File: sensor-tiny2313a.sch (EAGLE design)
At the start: 36 parts, among them M1 NRF24L01P-M, M2 DHT22-NP, Q2 IRLML2502, U1 TINY2313-*S*, U2 MCP1640C, X1 I2C, X2 serial

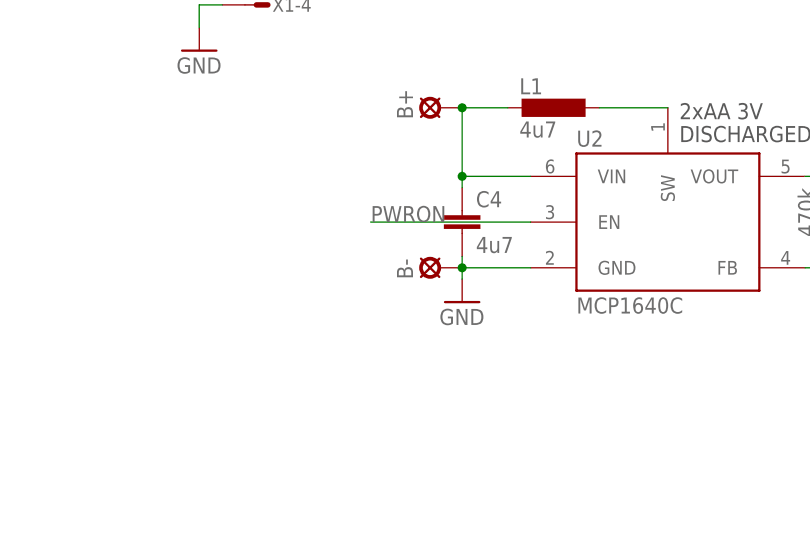
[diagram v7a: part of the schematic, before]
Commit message: pulldown for boostup enable line
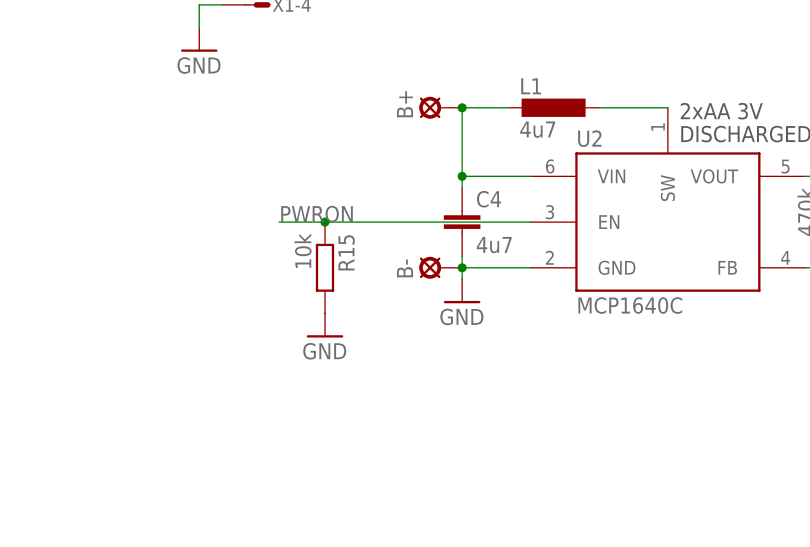
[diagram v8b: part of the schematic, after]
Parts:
- added R15: 10k, rcl:R-EU_R0603
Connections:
- net GND: now also R15.2
- net PWRON: now also R15.1
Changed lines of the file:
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@@
 <part name="U$3" library="creative-commons" deviceset="BY" device="-TPLACE-HS" value="BY-TPLACE-HS"/>
 <part name="U$4" library="creative-commons" deviceset="SA" device="-TPLACE-HALF" value="SA-TPLACE-HALF"/>
+<part name="R15" library="rcl" deviceset="R-EU_" device="R0603" value="10k"/>
+<part name="GND9" library="supply1" deviceset="GND" device=""/>
 </parts>
 <sheets>
@@
 <instance part="U$3" gate="G$1" x="222.25" y="20.32"/>
 <instance part="U$4" gate="G$1" x="227.33" y="20.32"/>
+<instance part="R15" gate="G$1" x="134.62" y="43.18" rot="R270"/>
+<instance part="GND9" gate="1" x="134.62" y="35.56"/>
 </instances>
 <busses>
@@
 <wire x1="120.65" y1="72.39" x2="120.65" y2="69.85" width="0.1524" layer="91"/>
 <pinref part="X1" gate="-4" pin="S"/>
+</segment>
+<segment>
+<pinref part="R15" gate="G$1" pin="2"/>
+<pinref part="GND9" gate="1" pin="GND"/>
 </segment>
 </net>
@@
 <segment>
 <pinref part="U2" gate="G$1" pin="EN"/>
-<wire x1="157.48" y1="48.26" x2="139.7" y2="48.26" width="0.1524" layer="91"/>
-<label x="139.7" y="48.26" size="1.778" layer="95"/>
-</segment>
-<segment>
+<wire x1="157.48" y1="48.26" x2="134.62" y2="48.26" width="0.1524" layer="91"/>
+<label x="129.54" y="48.26" size="1.778" layer="95"/>
+<pinref part="R15" gate="G$1" pin="1"/>
+<wire x1="134.62" y1="48.26" x2="129.54" y2="48.26" width="0.1524" layer="91"/>
+<junction x="134.62" y="48.26"/>
+</segment>
+<segment>
